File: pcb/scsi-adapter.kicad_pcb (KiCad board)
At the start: 4 copper layers, 120 x 90 mm, 412 parts, among them J101 Bench 5V, J201 TERMPWR jumper, J301 IDC50 box header, J302 HD50 female R/A, J303 2x17 box header, J401 TC2030-IDC, J501 TF PUSH, J601 USB-C (HRO TYPE-C-31-M-12), Q1001 FDV301N, Q1101 FDV301N, Q1201 FDV301N, Q1301 FDV301N, Q1401 FDV301N, Q1501 FDV301N, Q1601 FDV301N, Q1701 FDV301N, Q1801 FDV301N, Q1901 FDV301N, Q2001 FDV301N, Q201 2N7002, Q2101 FDV301N, Q2301 FDV301N, Q901 FDV301N, SW301 DIP 2-pos, SW401 BOOTSEL, SW402 RUN, U1001 74LVC1G17GW, U101 TPS259470ARPWR, U102 TPS2116DRLR, U103 TPS73701DCQR, U104 TPS73701DCQR, U1101 74LVC1G17GW, U1201 74LVC1G17GW, U1301 74LVC1G17GW, U1401 74LVC1G17GW, U1501 74LVC1G17GW, U1601 74LVC1G17GW, U1701 74LVC1G17GW, U1801 74LVC1G17GW, U1901 74LVC1G17GW, U2001 74LVC1G17GW, U201 TPS259470ARPWR, U202 LM393DR2G, U203 CJ431, U2101 74LVC1G17GW, U2201 74LVC1G17GW, U2301 74LVC1G17GW, U2401 74LVC1G17GW, U2501 74LVC1G17GW, U2601 74LVC1G17GW, U301 SN74LVTH245APWR, U302 SN74LVTH245APWR, U303 SN74LVTH245APWR, U401 RP2350B, U402 W25Q128JVSIQ, U403 APS6404L-3SQR-SN, U501 TCA9555PWR, U601 CH334P, U701 FT232HL, U702 93LC56BT-I/OT, U901 74LVC1G17GW, Y401 12MHz ABM8-272-T3, Y601 12MHz ABM8-272-T3, Y701 12MHz ABM8-272-T3

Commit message: rev 1
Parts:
- moved FT232H_3V3 3.41 mm to (115.8, 47.3)
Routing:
- net FT232H_3V3: track 80.2 -> 76.6 mm
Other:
- board text added: "SCSI to USB-C rev 1 Landon Carter MIT License"
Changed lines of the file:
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@@
 	(footprint "TestPoint:TestPoint_Pad_D1.5mm"
 		(layer "F.Cu")
-		(at 115 44 90)
+		(at 115.85 47.3 90)
 		(descr "SMD pad as test Point, diameter 1.5mm")
 		(tags "test point SMD pad")
@@
 		(layer "Edge.Cuts")
 	)
+	(gr_text "SCSI to USB-C\nrev 1\nLandon Carter\nMIT License\n"
+		(at 105.65 44 0)
+		(layer "F.SilkS")
+		(effects
+			(font
+				(size 1 1)
+				(thickness 0.15)
+			)
+			(justify left bottom)
+		)
+	)
 	(gr_text "BOOTSEL"
 		(at 134.1 104.35 0)
@@
 	)
 	(segment
-		(start 116.8 45.8)
-		(end 115 44)
-		(width 0.3)
-		(layer "F.Cu")
-		(net 194)
-	)
-	(segment
 		(start 107.8 59.2875)
 		(end 107.85 59.2375)
@@
 	)
 	(segment
+		(start 116.8 48.25)
+		(end 115.85 47.3)
+		(width 0.3)
+		(layer "F.Cu")
+		(net 194)
+	)
+	(segment
 		(start 108.9 53.9)
 		(end 108.29 53.9)
@@
 	)
 	(segment
+		(start 116.8 48.9)
+		(end 116.8 48.25)
+		(width 0.3)
+		(layer "F.Cu")
+		(net 194)
+	)
+	(segment
 		(start 110.88 55)
 		(end 111.83 55.95)
@@
 		(width 0.3)
 		(layer "F.Cu")
-		(net 194)
-	)
-	(segment
-		(start 116.8 48.9)
-		(end 116.8 45.8)
-		(width 0.3)
-		(layer "F.Cu")

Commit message: JLC text
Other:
- board text added: "JLCJLCJLCJLC"
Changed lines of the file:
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@@
+		)
+	)
+	(gr_text "JLCJLCJLCJLC"
+		(at 127.55 39 0)
+		(layer "F.SilkS")
+		(effects
+			(font
+				(size 1 1)
+				(thickness 0.15)
+			)
 		)
 	)

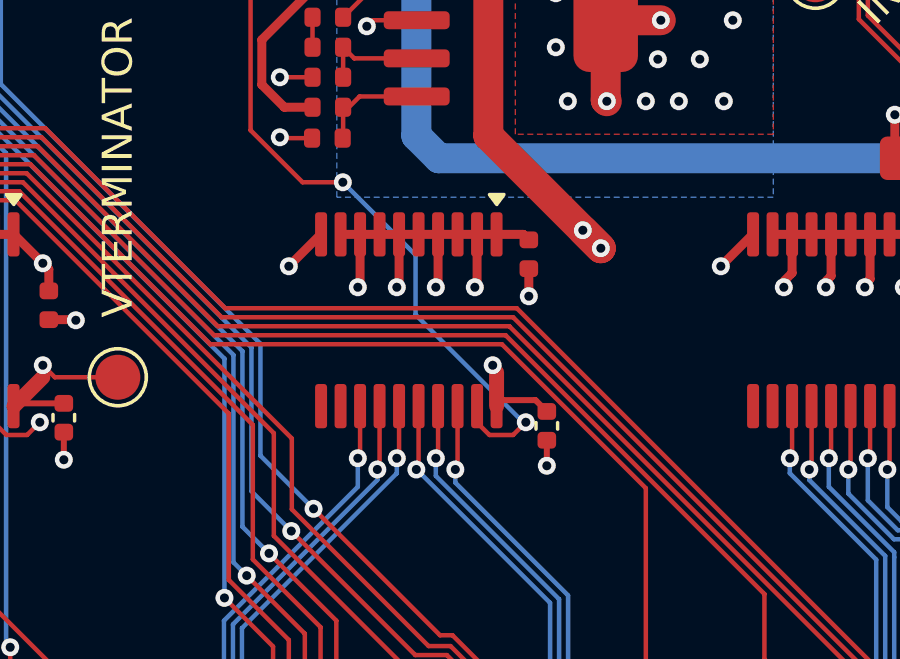
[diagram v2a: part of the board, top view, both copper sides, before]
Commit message: JLC order export script and first file set; C305 clearance fix
tools/jlc_export.py builds the Gerber/drill zip, BOM and CPL into pcb/fab from a
zone-refilled temp copy, and refuses to export if DRC or the BOM cross-checks fail.
The PCB change is the owner's zone refill and the clearance fix at C305 pad 1.
pcb/fab still lists C11616 for R101 (10 in stock at JLC); it is replaced next.
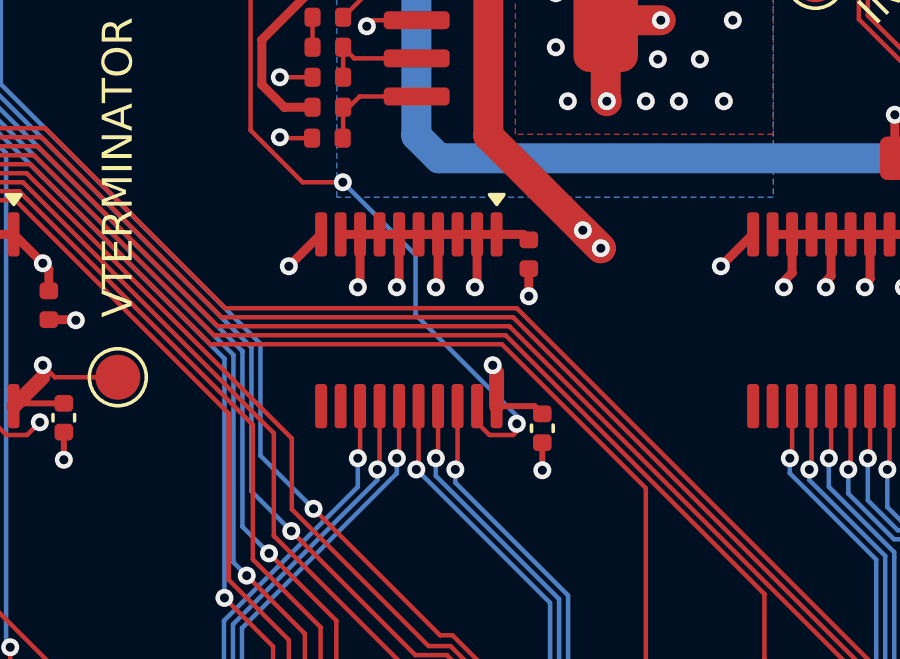
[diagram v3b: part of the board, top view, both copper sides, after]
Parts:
- moved C305 0.17 mm to (184.8, 77.2)
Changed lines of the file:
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@@
 	(footprint "Capacitor_SMD:C_0402_1005Metric"
 		(layer "F.Cu")
-		(at 185 77.12 -90)
+		(at 184.85 77.2 -90)
 		(descr "Capacitor SMD 0402 (1005 Metric), square (rectangular) end terminal, IPC-7351 nominal, (Body size source: IPC-SM-782 page 76, https://www.pcb-3d.com/wordpress/wp-content/uploads/ipc-sm-782a_amendment_1_and_2.pdf), generated with kicad-footprint-generator")
 		(tags "capacitor")
@@
 	)
 	(segment
+		(start 183.875 77.425)
+		(end 183.08761 77.425)
+		(width 0.15)
+		(layer "F.Cu")
+		(net 145)
+	)
+	(segment
 		(start 198.375 77)
 		(end 198.375 77.125)
@@
 	)
 	(segment
-		(start 184.3 77)
+		(start 184 77.3)
 		(end 183.875 77.425)
 		(width 0.15)
@@
 	)
 	(segment
+		(start 184 77.05)
+		(end 184 77.3)
+		(width 0.15)
+		(layer "F.Cu")
+		(net 145)
+	)
+	(segment
 		(start 175.125 67.267463)
 		(end 175.125 37.245)
@@
 	)
 	(segment
-		(start 182.675 77.01239)
-		(end 182.675 76.4625)
+		(start 183.08761 77.425)
+		(end 182.675 77.01239)
 		(width 0.15)
 		(layer "F.Cu")
@@
 	)
 	(segment
-		(start 183.08761 77.425)
-		(end 182.675 77.01239)
-		(width 0.15)
-		(layer "F.Cu")
-		(net 145)
-	)
-	(segment
-		(start 183.875 77.425)
-		(end 183.08761 77.425)
+		(start 182.675 77.01239)
+		(end 182.675 76.4625)
 		(width 0.15)
 		(layer "F.Cu")
@@
 	)
 	(via
-		(at 184.3 77)
+		(at 184 77.05)
 		(size 0.6)
 		(drill 0.3)
@@
 	)
 	(segment
-		(start 178.2 69)
+		(start 180.625 73.412958)
 		(end 180.625 71.425)
 		(width 0.15)
@@
 	)
 	(segment
-		(start 180.625 71.425)
-		(end 180.625 73.412958)
+		(start 184 77.05)
+		(end 184 76.787958)
 		(width 0.15)
 		(layer "B.Cu")
@@
 	)
 	(segment
-		(start 184.212042 77)
-		(end 184.3 77)
+		(start 184 76.787958)
+		(end 180.625 73.412958)
 		(width 0.15)
 		(layer "B.Cu")
@@
 	)
 	(segment
-		(start 180.625 73.412958)
-		(end 184.212042 77)
+		(start 180.625 71.425)
+		(end 178.2 69)
 		(width 0.15)
 		(layer "B.Cu")
@@
 	)
 	(segment
+		(start 183.95 77)
+		(end 184 77.05)
+		(width 0.15)
+		(layer "In2.Cu")
+		(net 145)
+	)
+	(segment
+		(start 184.05 77)
+		(end 184 77.05)
+		(width 0.15)
+		(layer "In2.Cu")
+		(net 145)
+	)
+	(segment
 		(start 168.1 77)
-		(end 184.3 77)
+		(end 183.95 77)
 		(width 0.15)
 		(layer "In2.Cu")
@@
 	(segment
 		(start 198.375 77)
-		(end 184.3 77)
+		(end 184.05 77)
 		(width 0.15)
 		(layer "In2.Cu")
@@
 	)
 	(segment
-		(start 185 77.6)
-		(end 185 78.45)
-		(width 0.2)
-		(layer "F.Cu")
-		(net 195)
-	)
-	(segment
 		(start 106.9 56.9625)
 		(end 106.9 55.6)
@@
 	)
 	(segment
+		(start 184.85 77.68)
+		(end 184.85 78.6)
+		(width 0.2)
+		(layer "F.Cu")
+		(net 195)
+	)
+	(segment
 		(start 107.235 78.435)
 		(end 108 79.2)
@@
 	)
 	(via
+		(at 184.85 78.6)
+		(size 0.6)
+		(drill 0.3)
+		(layers "F.Cu" "B.Cu")
+		(net 195)
+	)
+	(via
 		(at 159.638154 51.454992)
 		(size 0.6)
@@
 	)
 	(via
-		(at 185 78.45)
-		(size 0.6)
-		(drill 0.3)
-		(layers "F.Cu" "B.Cu")
-		(net 195)
-	)
-	(via
 		(at 191.080671 103.637436)
 		(size 0.6)
@@
 	)
 	(segment
+		(start 184.85 76.72)
+		(end 184.5925 76.4625)
+		(width 0.2)
+		(layer "F.Cu")
+		(net 245)
+	)
+	(segment
 		(start 182.675 72.425)
 		(end 182.6 72.5)
@@
 	)
 	(segment
-		(start 185 76.64)
-		(end 184.622501 76.262501)
-		(width 0.2)
-		(layer "F.Cu")
-		(net 245)
-	)
-	(segment
 		(start 197.725 75.125)
 		(end 197.7 75.1)
@@
 	)
 	(segment
+		(start 184.5925 76.4625)
+		(end 183.325 76.4625)
+		(width 0.2)
+		(layer "F.Cu")
+		(net 245)
+	)
+	(segment
 		(start 182.675 70.7375)
 		(end 182.675 72.425)
@@
 		(layer "F.Cu")
 		(net 245)
-	)
-	(segment
-		(start 184.622501 76.262501)
-		(end 183.524999 76.262501)
-		(width 0.2)
-		(layer "F.Cu")
-		(net 245)
-	)
-	(segment
-		(start 183.524999 76.262501)
-		(end 183.325 76.4625)
-		(width 0.2)
-		(layer "F.Cu")
-		(net 245)
